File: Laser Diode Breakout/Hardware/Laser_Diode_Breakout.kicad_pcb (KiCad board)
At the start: 2 copper layers, 29.2 x 35.6 mm, 10 parts, among them Q1 BSS138, Q2 BSS138

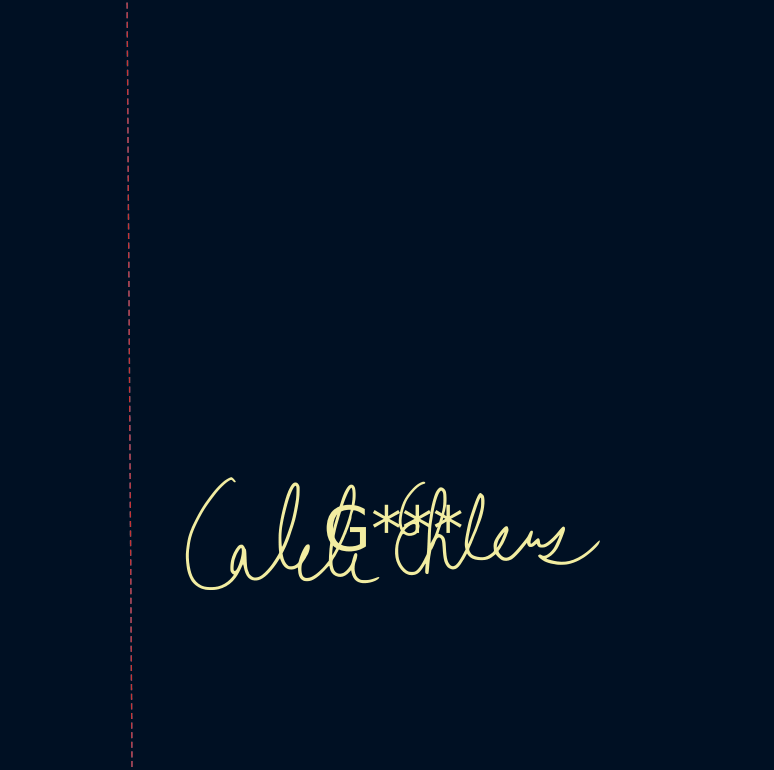
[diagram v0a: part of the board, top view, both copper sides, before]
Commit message: added label to raman board
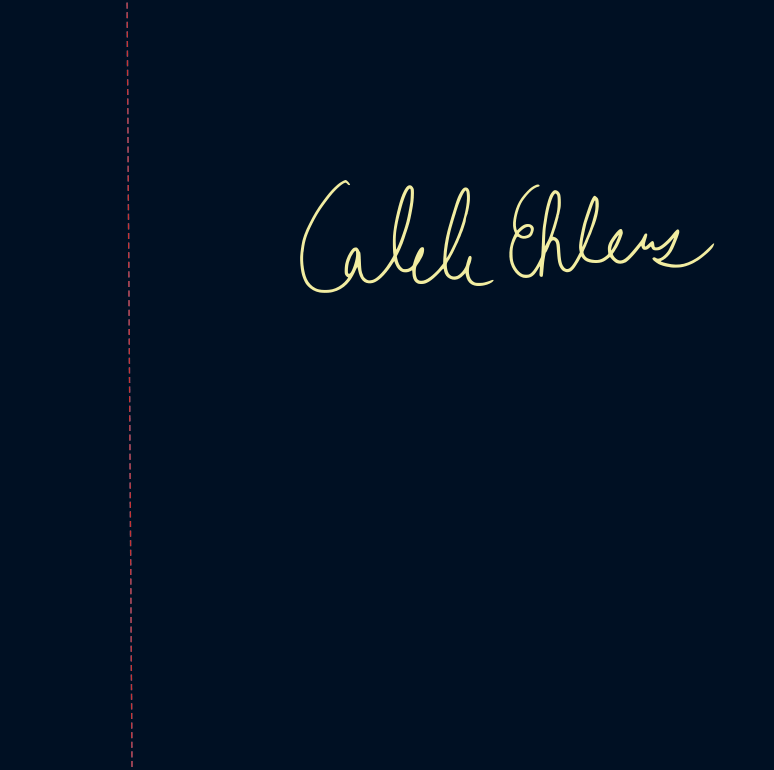
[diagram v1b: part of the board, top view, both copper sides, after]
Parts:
- moved G*** 10.6 mm to (78.0, 38.4)
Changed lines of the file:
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@@
   )
   (footprint "Signatures:Caleb_Ehlers_Signature_15mmx4.8mm" (layer "F.Cu")
-    (at 74.168 48.26)
+    (at 77.978 38.354)
     (attr board_only exclude_from_pos_files exclude_from_bom)
-    (fp_text reference "G***" (at 0 0) (layer "F.SilkS")
+    (fp_text reference "G***" (at 1.016 -5.842) (layer "F.SilkS") hide
         (effects (font (size 1.5 1.5) (thickness 0.3)))
     )

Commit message: finish diode breakout changes
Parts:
- added V3: Via, MRDT_Drill_Holes:4_40_Hole, F.Cu at (36.3, 33.5)
- added V4: Via, MRDT_Drill_Holes:4_40_Hole, F.Cu at (61.7, 58.9)
- D1: value 785nm Laser Diode -> 782nm Laser Diode
- moved G*** 40.4 mm to (38.4, 46.2), turned to -90 degrees
- moved R2 12.5 mm to (59.4, 42.4), turned to -90 degrees
- moved D1 12.4 mm to (53.1, 44.2), turned to 90 degrees
- moved Q2 11.6 mm to (44.0, 42.9)
- moved D2 9.88 mm to (52.8, 51.3), turned to 90 degrees
- moved Q1 9.58 mm to (43.5, 49.8)
- moved R1 9.32 mm to (59.9, 50.0), turned to -90 degrees
- moved V1 9.25 mm to (61.7, 33.5)
- moved Conn1 8.44 mm to (52.3, 35.3)
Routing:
- net Red_LED: track 24.6 -> 14.1 mm
- net Green_LED: track 12.0 -> 18.7 mm
- net +12V: track 26.7 -> 20.8 mm
- net Net-(D2-A): track 5.57 -> 7.25 mm
- net Net-(D1-A): track 7.07 -> 5.51 mm
- net Net-(D1-K): track 7.48 -> 8.65 mm
- net Net-(D2-K): track 9.99 -> 9.02 mm
- net GND: vias 4 -> 2
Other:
- board size 29.2 x 35.6 mm -> 38.1 x 38.1 mm
- board text added: "520nm Green Diode"
- board text added: "782nm Red Diode"
- board text added: "Diode Breakout"

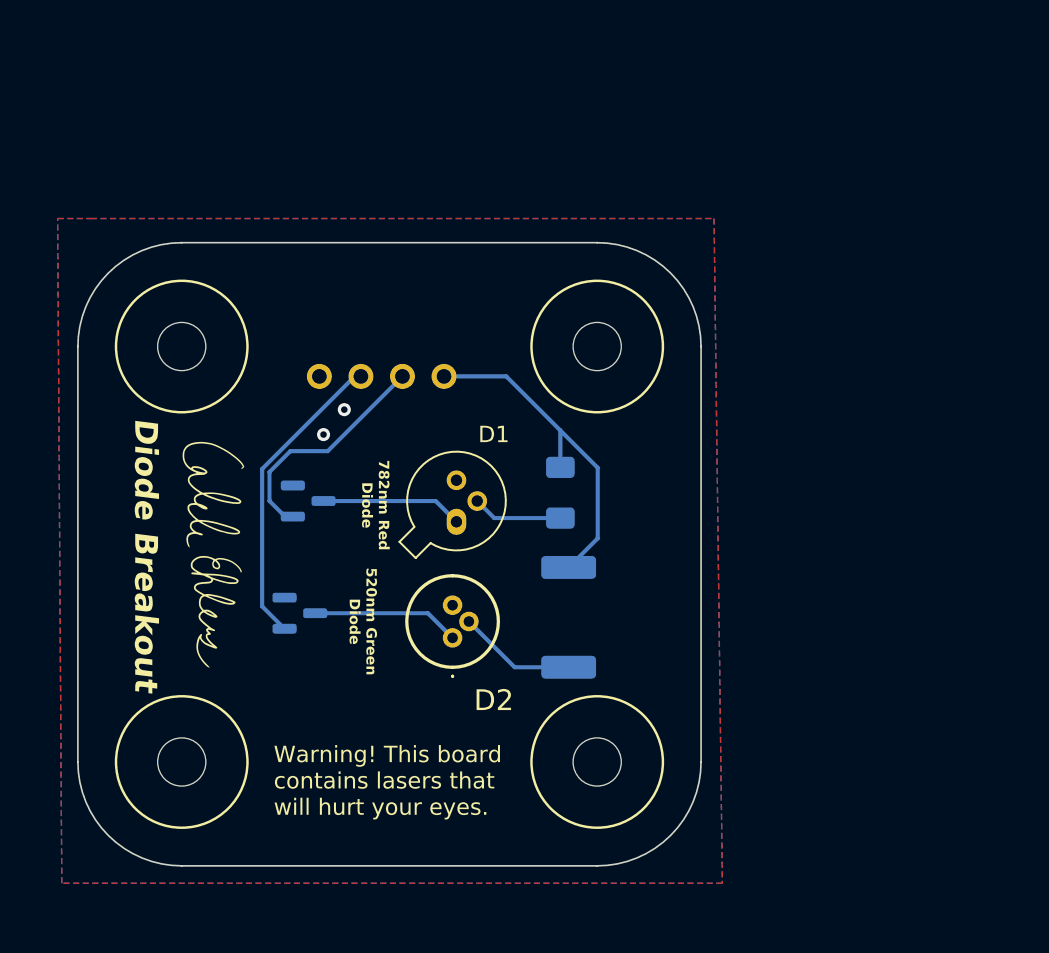
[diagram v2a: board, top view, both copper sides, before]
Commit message: adjusted page sizes for all boards
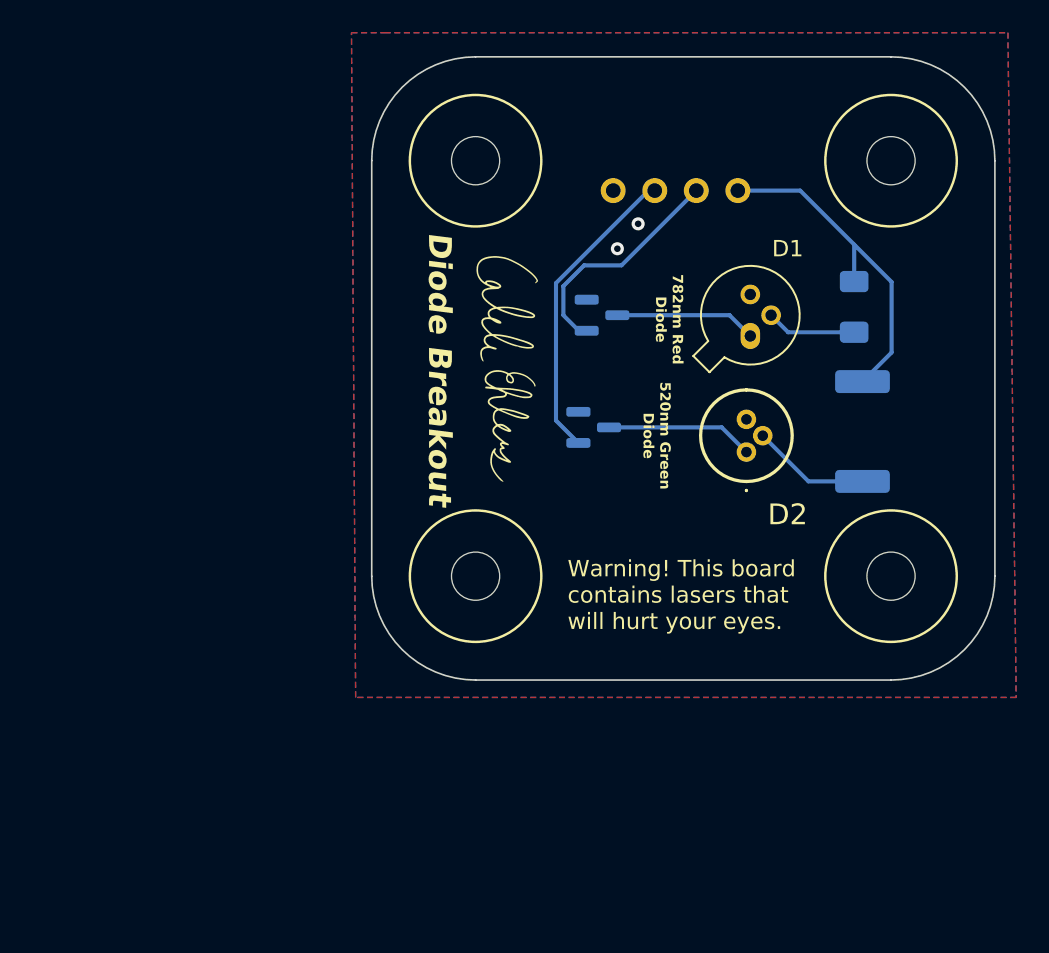
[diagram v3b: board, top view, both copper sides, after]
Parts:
- moved D2 21.3 mm to (70.8, 39.9)
- moved G*** 21.3 mm to (56.3, 34.9)
- moved R1 21.3 mm to (77.9, 38.7)
- moved V2 21.3 mm to (54.3, 47.5)
- moved Conn1 21.3 mm to (70.3, 23.9)
- moved D1 21.3 mm to (71.1, 32.8)
- moved Q2 21.3 mm to (62.0, 31.6)
- moved V1 21.3 mm to (79.7, 22.1)
- moved V4 21.3 mm to (79.7, 47.5)
- moved Q1 21.3 mm to (61.5, 38.4)
- moved R2 21.3 mm to (77.4, 31.1)
- moved V3 21.3 mm to (54.3, 22.1)
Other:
- outline, holes or cut-outs redrawn

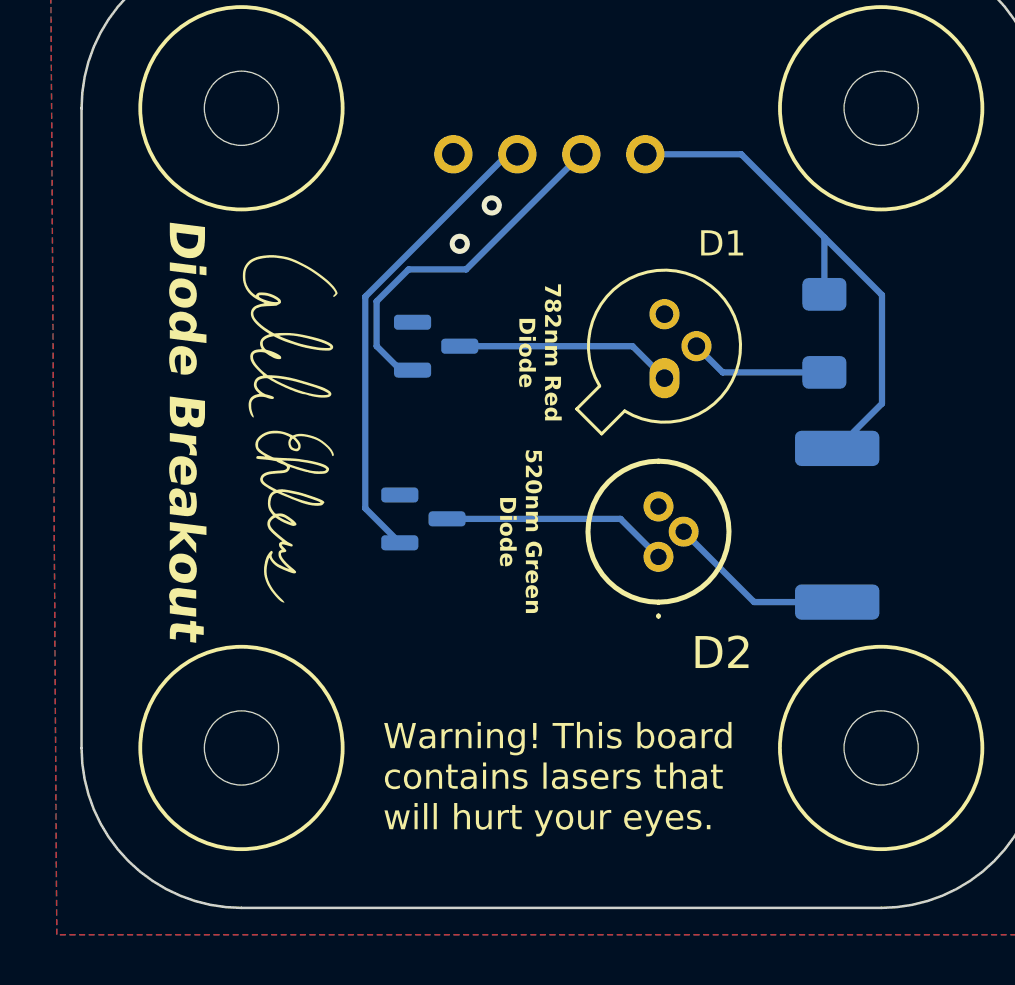
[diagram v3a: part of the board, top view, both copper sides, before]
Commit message: adjust silkscreen on diode board
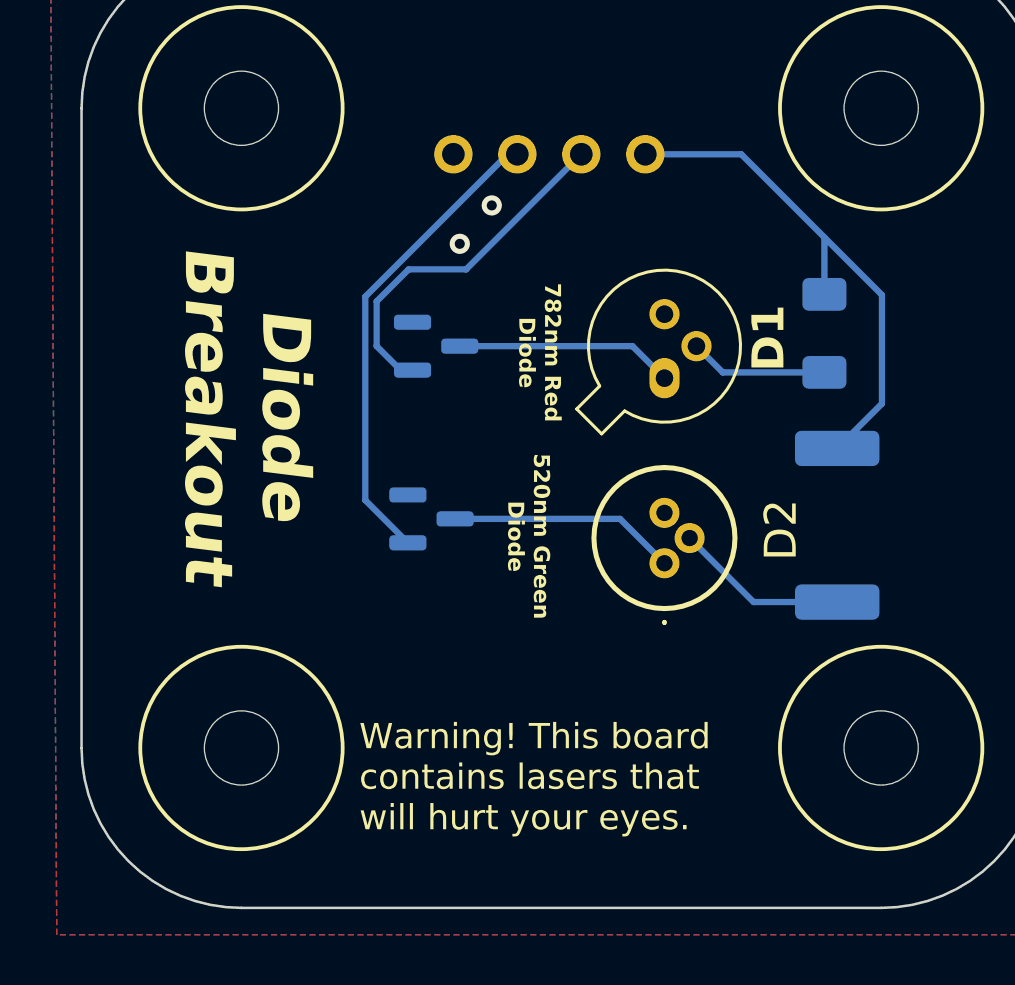
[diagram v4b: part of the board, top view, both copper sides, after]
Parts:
- G***: moved to B.Cu
- moved G*** 26.5 mm to (82.8, 35.6)
- moved D2 0.35 mm to (71.0, 40.2)
- moved Q1 0.32 mm to (61.8, 38.4)

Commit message: fixed board name silkscreens
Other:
- board text added: "Diode Breakout, Rev1 Mars Rover Design Team Missouri S&T, 2023 Caleb Ehlers"
- board text removed: "Diode Breakout"
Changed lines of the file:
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@@
     (effects (font (size 0.635 0.635) (thickness 0.127) bold) (justify bottom mirror))
-  )
-  (gr_text "Diode\nBreakout" (at 56.642 34.036 -270) (layer "B.SilkS")
-    (effects (font (size 1.905 1.905) (thickness 0.3048) bold italic) (justify bottom mirror))
   )
   (gr_text "Warning! This board\ncontains lasers that\nwill hurt your eyes." (at 58.928 50.869276) (layer "F.SilkS")
     (effects (font (size 1 1) (thickness 0.15)) (justify left bottom))
   )
-  (gr_text "Diode\nBreakout" (at 51.816 34.29 270) (layer "F.SilkS")
-    (effects (font (size 1.905 1.905) (thickness 0.3048) bold italic) (justify bottom))
+  (gr_text "Diode Breakout, Rev1\nMars Rover Design Team\nMissouri S&T, 2023\nCaleb Ehlers" (at 51.562 34.798 270) (layer "F.SilkS")
+    (effects (font (size 0.8636 0.8636) (thickness 0.1778) bold) (justify bottom))
   )
   (gr_text "782nm Red\nDiode" (at 65.208724 31.819276 -90) (layer "F.SilkS")
